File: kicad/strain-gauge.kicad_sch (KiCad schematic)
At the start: 0 parts

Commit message: first pass at testing board schematic, except amplifier wiring
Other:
- added sheet ADC (adc.kicad_sch)
- added sheet Amplifier (amplifier.kicad_sch)
- added sheet Counter (counter.kicad_sch)
- added sheet Multiplexer (multiplexer.kicad_sch)
- added sheet Pins (pins.kicad_sch)

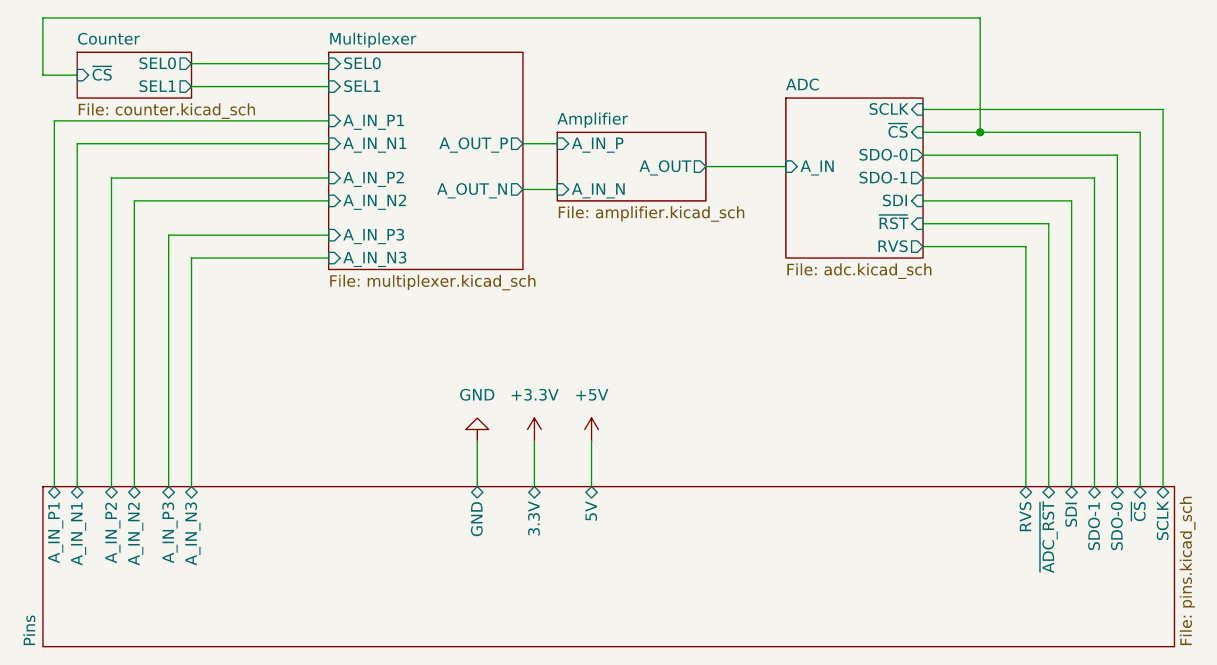
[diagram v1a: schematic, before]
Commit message: finish schematic for amp, and start routing (schematic isn't actually fully connected yet tho...)
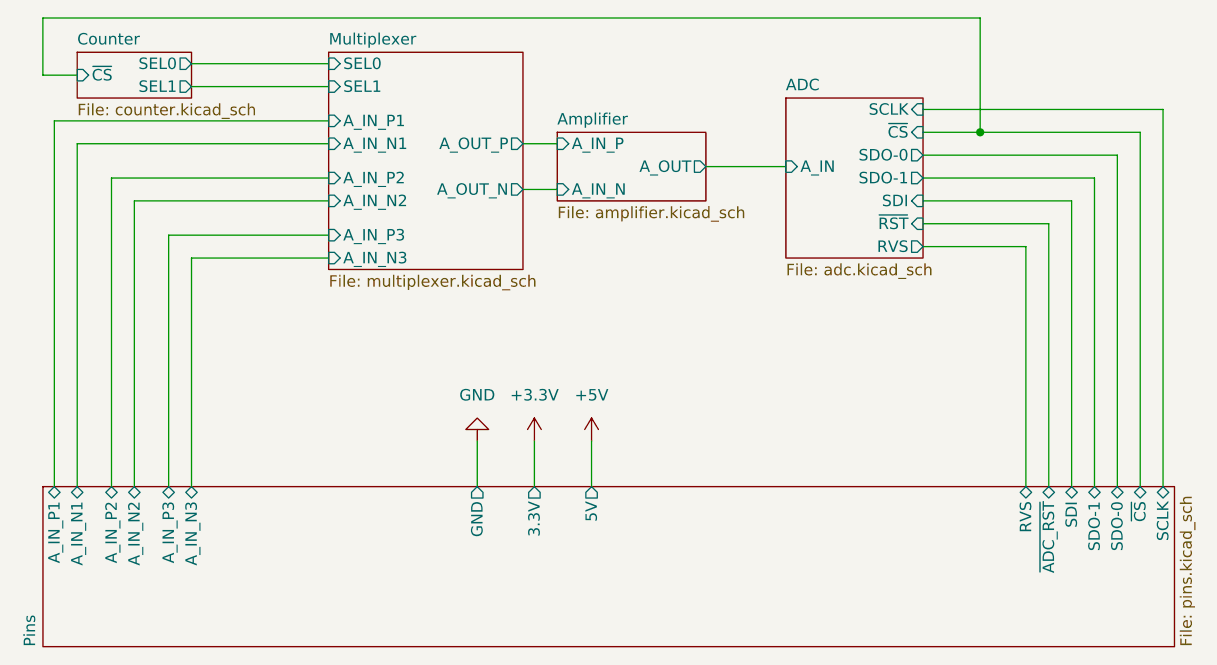
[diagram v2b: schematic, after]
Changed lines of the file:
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@@
 		(dnp no)
 		(fields_autoplaced yes)
-		(property "Reference" "#PWR013"
+		(property "Reference" "#PWR03"
 			(at 161.29 125.73 0)
 			(effects
@@
 			(project ""
 				(path "/cbc99ef0-5fa7-4678-bd4c-c2c08fe588b6"
-					(reference "#PWR013")
+					(reference "#PWR03")
 					(unit 1)
 				)
@@
 		(dnp no)
 		(fields_autoplaced yes)
-		(property "Reference" "#PWR012"
+		(property "Reference" "#PWR02"
 			(at 154.94 125.73 0)
 			(effects
@@
 			(project ""
 				(path "/cbc99ef0-5fa7-4678-bd4c-c2c08fe588b6"
-					(reference "#PWR012")
+					(reference "#PWR02")
 					(unit 1)
 				)
@@
 		(dnp no)
 		(fields_autoplaced yes)
-		(property "Reference" "#PWR011"
+		(property "Reference" "#PWR01"
 			(at 148.59 115.57 0)
 			(effects
@@
 			(project ""
 				(path "/cbc99ef0-5fa7-4678-bd4c-c2c08fe588b6"
-					(reference "#PWR011")
+					(reference "#PWR01")
 					(unit 1)
 				)
@@
 			)
 		)
-		(pin "GND" bidirectional
-			(at 148.59 127 90)
-			(effects
-				(font
-					(size 1.27 1.27)
-				)
-				(justify right)
-			)
-		)
 		(pin "A_IN_P2" bidirectional
 			(at 107.95 127 90)
@@
 			)
 		)
-		(pin "3.3V" bidirectional
-			(at 154.94 127 90)
-			(effects
-				(font
-					(size 1.27 1.27)
-				)
-				(justify right)
-			)
-		)
 		(pin "SDO-0" bidirectional
 			(at 219.71 127 90)
@@
 			)
 		)
-		(pin "5V" bidirectional
-			(at 161.29 127 90)
-			(effects
-				(font
-					(size 1.27 1.27)
-				)
-				(justify right)
-			)
-		)
 		(pin "A_IN_N1" bidirectional
 			(at 104.14 127 90)
@@
 			(effects
 				(font
+					(size 1.27 1.27)
+				)
+				(justify right)
+			)
+		)
+		(pin "GND" output
+			(at 148.59 127 90)
+			(effects
+				(font
+					(size 1.27 1.27)
+				)
+				(justify right)
+			)
+		)
+		(pin "3.3V" output
+			(at 154.94 127 90)
+			(effects
+				(font
+					(size 1.27 1.27)
+				)
+				(justify right)
+			)
+		)
+		(pin "5V" output
+			(at 161.29 127 90)
+			(effects
+				(font
